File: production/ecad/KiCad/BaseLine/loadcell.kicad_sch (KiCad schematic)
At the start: 10 parts, among them J1 LoadCell Connector, U1 ADS122C04IPW

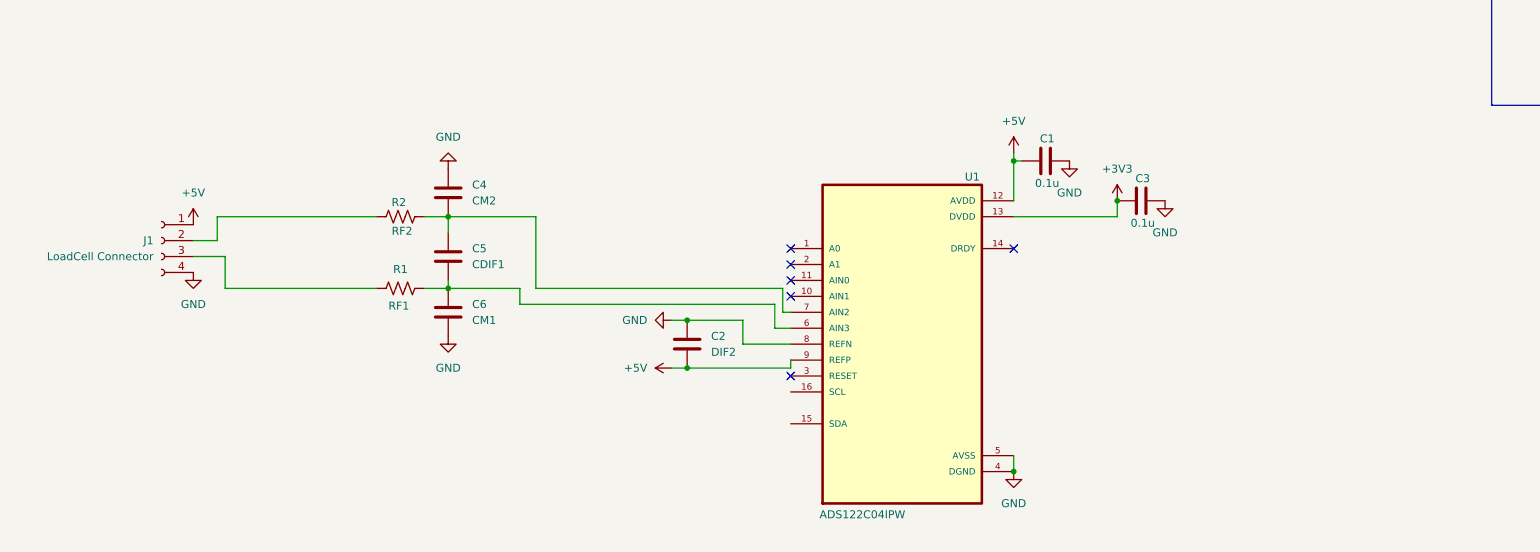
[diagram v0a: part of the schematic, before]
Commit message: Added vibe motor connector and amp I2C
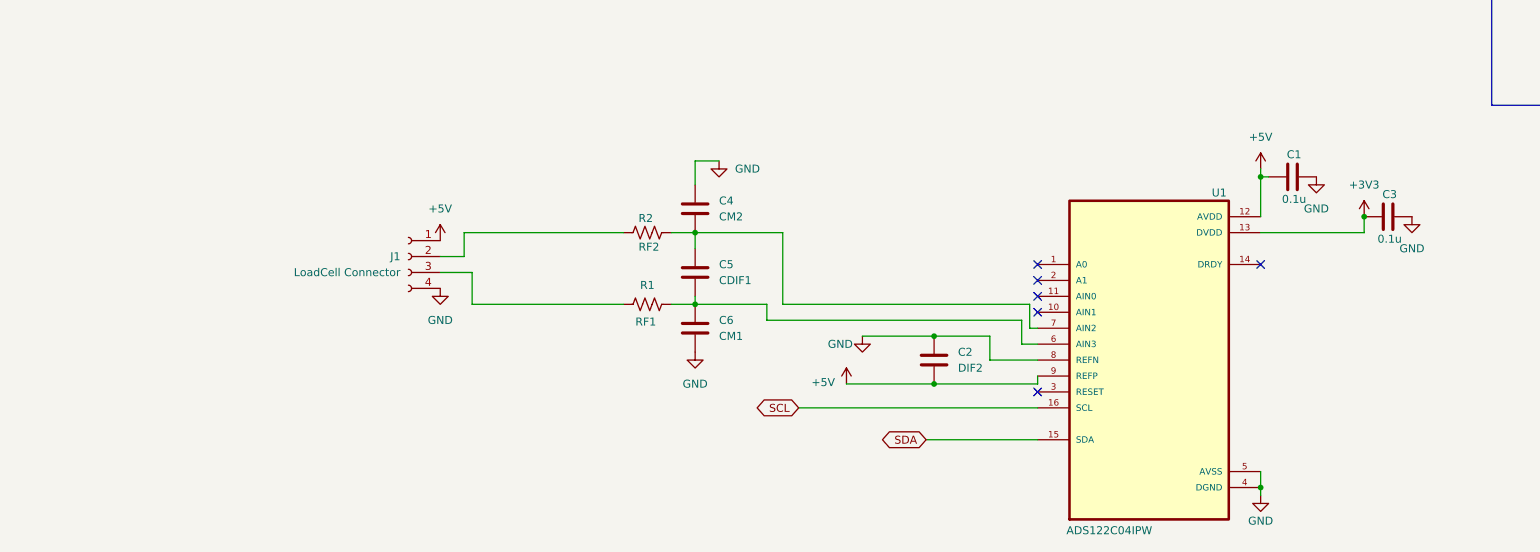
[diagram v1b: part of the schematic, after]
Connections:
- net SDA: now reaches U1.15 (SDA)
- net SCL: now reaches U1.16 (SCL)
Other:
- moved on the sheet: C1, C2, C3, C4, C5, C6, J1, R1, R2, U1

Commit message: Small changes
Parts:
- J1: value LoadCell Connector -> FX1901-0001-0200-L
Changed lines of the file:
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@@
 			)
 		)
-		(property "Value" "LoadCell Connector"
+		(property "Value" "FX1901-0001-0200-L"
 			(at 66.04 88.8999 0)
 			(effects
@@
 			)
 		)
-		(property "Datasheet" "~"
+		(property "Datasheet" "https://www.digikey.com/en/products/detail/te-connectivity-measurement-specialties/FX1901-0001-0200-L/5277314"
 			(at 67.31 86.36 0)
 			(effects

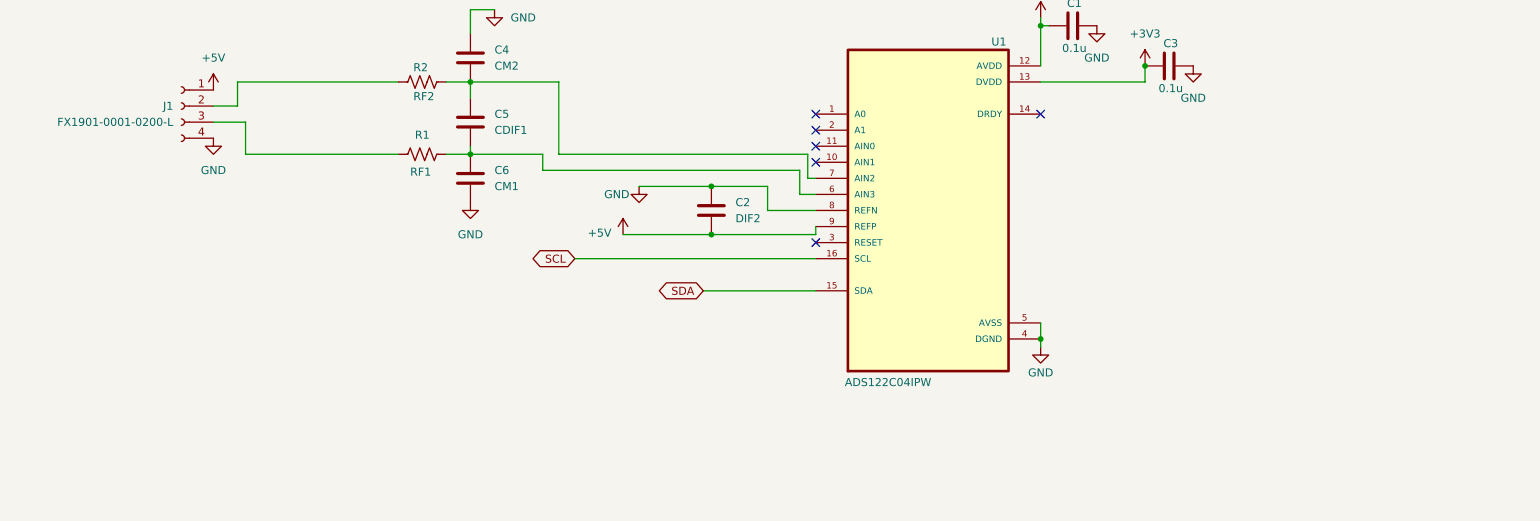
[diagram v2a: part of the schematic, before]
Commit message: Updated with new load cell amp IC
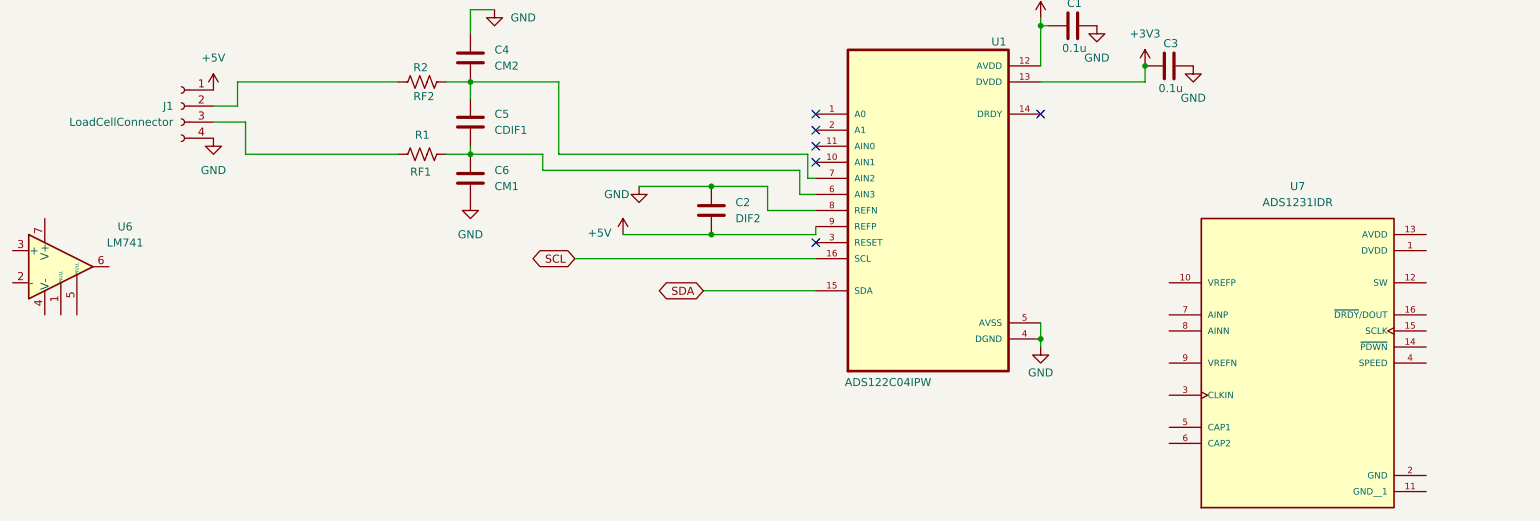
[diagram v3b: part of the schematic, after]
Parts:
- added U6: LM741, symbol Amplifier_Operational:LM741
- added U7: ADS1231IDR, ADS1231IDR:SOIC127P600X175-16N, symbol ADS1231IDR:ADS1231IDR
- J1: value FX1901-0001-0200-L -> LoadCellConnector

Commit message: Load Cell changes
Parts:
- removed C1, C3: 0.1u, symbol Device:C
- removed C2: DIF2, symbol Device:C
- removed C4: CM2, symbol Device:C
- removed C5: CDIF1, symbol Device:C
- removed C6: CM1, symbol Device:C
- removed R1: RF1, symbol Device:R_US
- removed R2: RF2, symbol Device:R_US
- removed U1: ADS122C04IPW, ADS122C04IPW:SOP65P640X120-16N, symbol ADS122C04IPW:ADS122C04IPW
- removed U6: LM741, symbol Amplifier_Operational:LM741
- added C16, C17: C, symbol Device:C
- added R23, R24, R25, R26: R_US, symbol Device:R_US
- added U6, U8: MIC920YC5-TR, SC-70_C5_MCH, symbol 2024-10-08_01-43-59:MIC920YC5-TR
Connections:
- net +5V: now also U6.5 (V+), U8.5 (V+)
- net GND: now also U6.2 (V-), U8.2 (V-)
- net RawLoadCell_-: now reaches J1.3 (Pin_3)
- net RawLoadCell_-: now also R25.2
- net RawLoadCell_+: now reaches J1.2 (Pin_2)
- net RawLoadCell_+: now also R23.2
- net LP_+: now reaches U7.7 (AINP)
- net LP_+: now also C16.2, U8.3 (IN-), U8.4 (OUT)
- net LP_-: now reaches U7.8 (AINN)
- net LP_-: now also C17.2, U6.3 (IN-), U6.4 (OUT)
- new net: R26.1, U6.1 (IN+)
- new net: C17.1, R25.1, R26.2
- new net: C16.1, R23.1, R24.2
- new net: R24.1, U8.1 (IN+)
- no-connect marks 6 -> 0
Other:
- note added: "Load Cell Low Pass Filtering"
- moved on the sheet: J1, U7

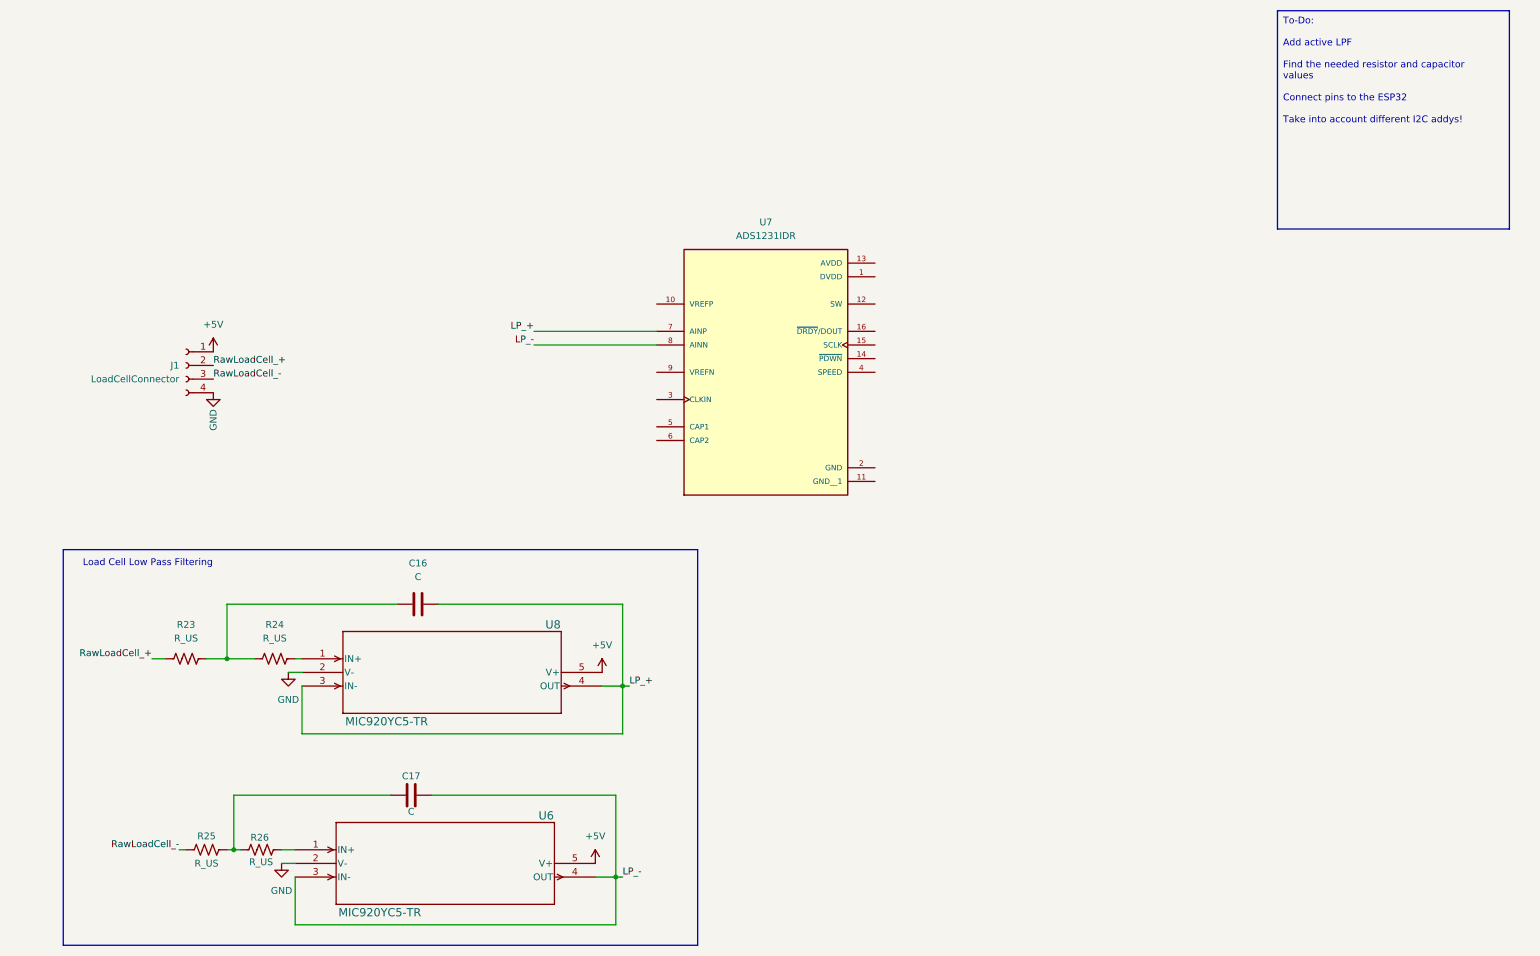
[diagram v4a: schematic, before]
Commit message: Added load cell amp schematic
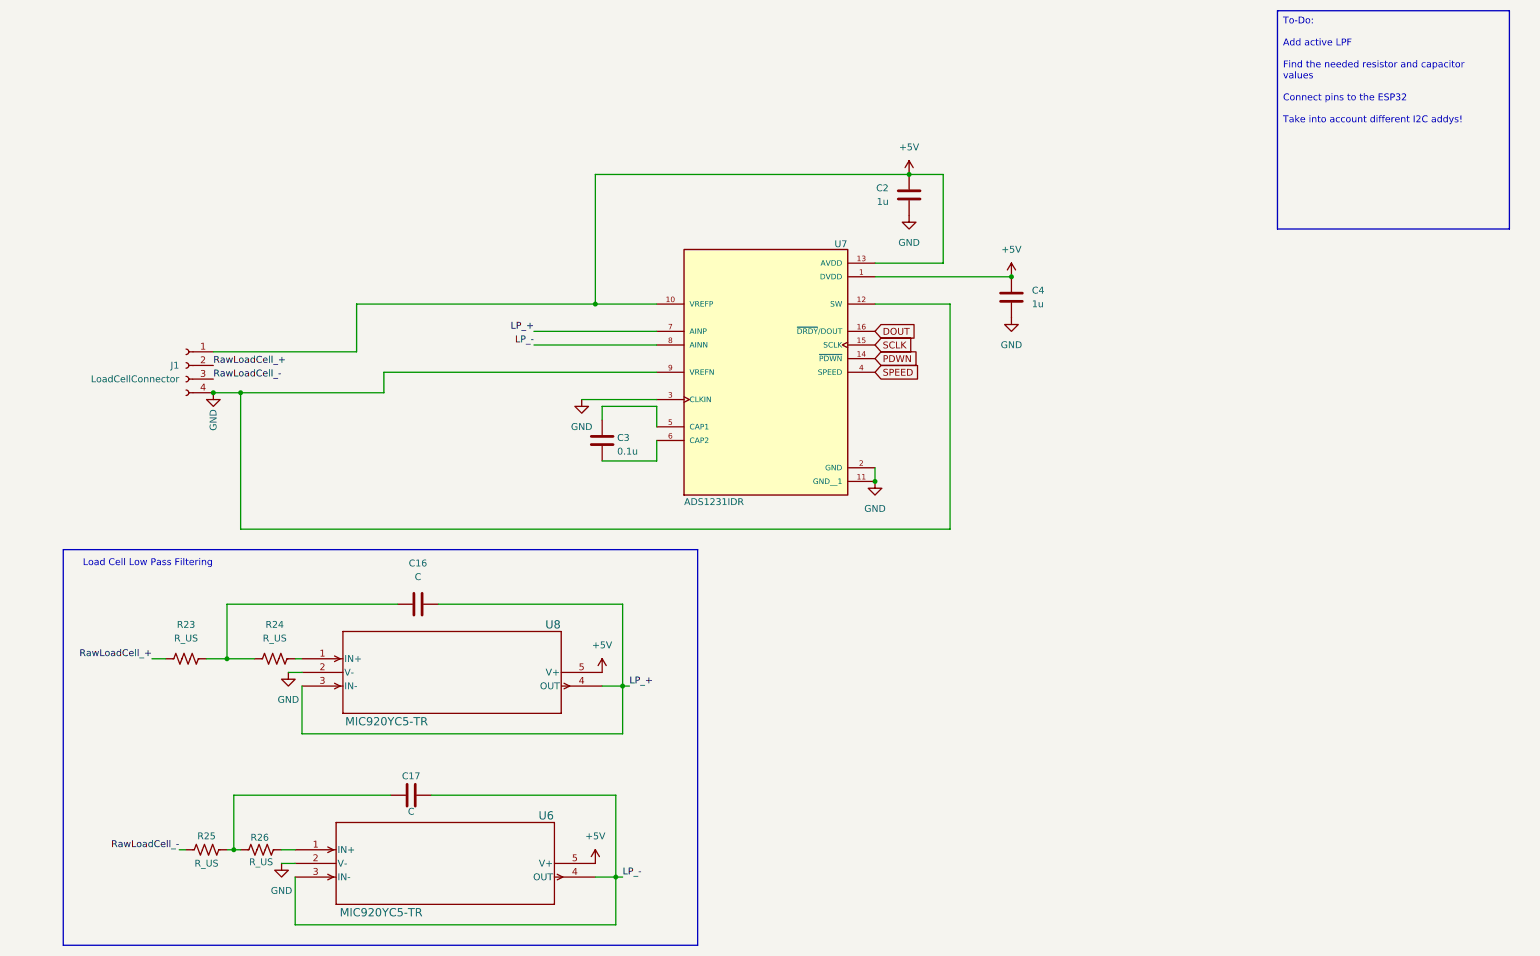
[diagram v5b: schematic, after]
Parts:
- added C2, C4: 1u, symbol Device:C
- added C3: 0.1u, symbol Device:C
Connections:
- net +5V: now also U7.1 (DVDD), U7.10 (VREFP), U7.13 (AVDD), C2.1, C4.1
- net GND: now also U7.11 (GND__1), U7.12 (SW), U7.2 (GND), U7.3 (CLKIN), U7.9 (VREFN), C2.2, C4.2
- net PDWN: now reaches U7.14 (~{PDWN})
- net SCLK: now reaches U7.15 (SCLK)
- net DOUT: now reaches U7.16 (~{DRDY}/DOUT)
- net SPEED: now reaches U7.4 (SPEED)
- net at U7.5 (CAP1): now also C3.1
- net at U7.6 (CAP2): now also C3.2

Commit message: Updates
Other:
- note removed: "Load Cell Low Pass Filtering"
- moved on the sheet: C2
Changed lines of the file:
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@@
 	)
 	(junction
-		(at 45.72 177.8)
+		(at 73.66 92.71)
 		(diameter 0)
 		(color 0 0 0 0)
 	)
 	(junction
-		(at 171.45 52.07)
+		(at 45.72 177.8)
 		(diameter 0)
 		(color 0 0 0 0)
@@
 	)
 	(junction
-		(at 46.99 92.71)
+		(at 177.8 52.07)
+		(diameter 0)
+		(color 0 0 0 0)
+	)
+	(junction
+		(at 185.42 52.07)
 		(diameter 0)
 		(color 0 0 0 0)
@@
 	(wire
 		(pts
+			(xy 185.42 52.07) (xy 177.8 52.07)
+		)
+		(stroke
+			(width 0)
+			(type default)
+		)
+	)
+	(wire
+		(pts
 			(xy 57.15 142.24) (xy 58.42 142.24)
 		)
@@
 	(wire
 		(pts
-			(xy 113.03 52.07) (xy 171.45 52.07)
+			(xy 113.03 52.07) (xy 177.8 52.07)
 		)
 		(stroke
@@
 	(wire
 		(pts
-			(xy 46.99 92.71) (xy 41.91 92.71)
+			(xy 41.91 92.71) (xy 73.66 92.71)
 		)
 		(stroke
@@
 	(wire
 		(pts
-			(xy 73.66 88.9) (xy 73.66 92.71)
+			(xy 73.66 88.9) (xy 124.46 88.9)
 		)
 		(stroke
@@
 	(wire
 		(pts
-			(xy 73.66 92.71) (xy 46.99 92.71)
+			(xy 114.3 97.79) (xy 114.3 95.25)
 		)
 		(stroke
@@
 	(wire
 		(pts
-			(xy 114.3 97.79) (xy 114.3 95.25)
+			(xy 57.15 182.88) (xy 57.15 191.77)
 		)
 		(stroke
@@
 	(wire
 		(pts
-			(xy 57.15 182.88) (xy 57.15 191.77)
+			(xy 30.48 142.24) (xy 33.02 142.24)
 		)
 		(stroke
@@
 	(wire
 		(pts
-			(xy 30.48 142.24) (xy 33.02 142.24)
+			(xy 40.64 142.24) (xy 44.45 142.24)
 		)
 		(stroke
@@
 	(wire
 		(pts
-			(xy 40.64 142.24) (xy 44.45 142.24)
+			(xy 165.1 71.12) (xy 190.5 71.12)
 		)
 		(stroke
@@
 	(wire
 		(pts
-			(xy 165.1 71.12) (xy 190.5 71.12)
+			(xy 116.84 182.88) (xy 116.84 191.77)
 		)
 		(stroke
@@
 	(wire
 		(pts
-			(xy 116.84 182.88) (xy 116.84 191.77)
+			(xy 73.66 92.71) (xy 73.66 88.9)
 		)
 		(stroke
@@
 	(wire
 		(pts
-			(xy 179.07 118.11) (xy 46.99 118.11)
+			(xy 179.07 118.11) (xy 73.66 118.11)
 		)
 		(stroke
@@
 	(wire
 		(pts
-			(xy 124.46 88.9) (xy 73.66 88.9)
-		)
-		(stroke
-			(width 0)
-			(type default)
-		)
-	)
-	(wire
-		(pts
 			(xy 110.49 93.98) (xy 124.46 93.98)
 		)
@@
 	(wire
 		(pts
-			(xy 46.99 118.11) (xy 46.99 92.71)
+			(xy 73.66 92.71) (xy 73.66 118.11)
 		)
 		(stroke
@@
 	(wire
 		(pts
-			(xy 171.45 52.07) (xy 177.8 52.07)
-		)
-		(stroke
-			(width 0)
-			(type default)
-		)
-	)
-	(wire
-		(pts
 			(xy 101.6 83.82) (xy 124.46 83.82)
 		)
@@
 		)
 	)
-	(rectangle
-		(start 13.97 121.92)
-		(end 132.08 195.58)
-		(stroke
-			(width 0)
-			(type default)
-		)
-		(fill
-			(type none)
-		)
-	)
 	(image
 		(at 64.77 43.18)
@@
 		)
 	)
-	(text_box "To-Do: \n\nAdd active LPF\n\nFind the needed resistor and capacitor values\n\nConnect pins to the ESP32\n\nTake into account different I2C addys!"
+	(text_box "Load Cell Low Pass Filtering\n"
 		(exclude_from_sim no)
-		(at 240.03 21.59 0)
-		(size 43.18 40.64)
+		(at 13.97 120.65 0)
+		(size 120.65 74.93)
 		(stroke
 			(width 0)
@@
 		)
 	)
-	(text "Load Cell Low Pass Filtering"
+	(text_box "To-Do: \n\nFind the needed resistor and capacitor values\n\nHow do you connect to ESP32?\n"
 		(exclude_from_sim no)
-		(at 29.718 124.46 0)
+		(at 240.03 21.59 0)
+		(size 43.18 40.64)
+		(stroke
+			(width 0)
+			(type default)
+		)
+		(fill
+			(type none)
+		)
 		(effects
 			(font
 				(size 1.27 1.27)
 			)
+			(justify left top)
 		)
 	)
@@
 		(on_board yes)
 		(dnp no)
-		(fields_autoplaced yes)
 		(property "Reference" "#PWR051"
 			(at 54.61 186.69 0)
@@
 		)
 		(property "Value" "GND"
-			(at 54.61 185.42 0)
+			(at 54.61 184.15 0)
 			(effects
 				(font
@@
 	)
 	(symbol
+		(lib_name "MIC920YC5-TR_1")
 		(lib_id "2024-10-08_01-43-59:MIC920YC5-TR")
 		(at 58.42 142.24 0)
@@
 	(symbol
 		(lib_id "Device:C")
-		(at 171.45 55.88 0)
+		(at 185.42 55.88 0)
 		(mirror y)
 		(unit 1)
@@
 		(dnp no)
 		(property "Reference" "C2"
-			(at 167.64 54.6099 0)
+			(at 181.61 54.6099 0)
 			(effects
 				(font
@@
 		)
 		(property "Value" "1u"
-			(at 167.64 57.1499 0)
+			(at 181.61 57.1499 0)
 			(effects
 				(font
@@
 		)
 		(property "Footprint" ""
-			(at 170.4848 59.69 0)
+			(at 184.4548 59.69 0)
 			(effects
 				(font
@@
 		)
 		(property "Datasheet" "~"
-			(at 171.45 55.88 0)
+			(at 185.42 55.88 0)
 			(effects
 				(font
@@
 		)
 		(property "Description" "Unpolarized capacitor"
-			(at 171.45 55.88 0)
+			(at 185.42 55.88 0)
 			(effects
 				(font
@@
 		(on_board yes)
 		(dnp no)
-		(fields_autoplaced yes)
 		(property "Reference" "#PWR049"
 			(at 55.88 151.13 0)
@@
 		)
 		(property "Value" "GND"
-			(at 55.88 149.86 0)
+			(at 55.88 148.082 0)
 			(effects
 				(font
@@
 	(symbol
 		(lib_id "power:GND")
-		(at 171.45 59.69 0)
+		(at 185.42 59.69 0)
 		(unit 1)
 		(exclude_from_sim no)
@@
 		(on_board yes)
 		(dnp no)
-		(fields_autoplaced yes)
 		(property "Reference" "#PWR04"
-			(at 171.45 66.04 0)
+			(at 185.42 66.04 0)
 			(effects
 				(font
@@
 		)
 		(property "Value" "GND"
-			(at 171.45 64.77 0)
+			(at 185.674 63.754 0)
 			(effects
 				(font
@@
 		)
 		(property "Footprint" ""
-			(at 171.45 59.69 0)
+			(at 185.42 59.69 0)
 			(effects
 				(font
@@
 		)
 		(property "Datasheet" ""
-			(at 171.45 59.69 0)
+			(at 185.42 59.69 0)
 			(effects
 				(font
@@
 		)
 		(property "Description" "Power symbol creates a global label with name \"GND\" , ground"
-			(at 171.45 59.69 0)
+			(at 185.42 59.69 0)
 			(effects
 				(font
@@
 		)
 		(property "Value" "GND"
-			(at 41.91 97.79 90)
+			(at 41.91 96.266 0)
 			(effects
 				(font
@@
 	(symbol
 		(lib_id "power:+5V")
-		(at 171.45 52.07 0)
+		(at 185.42 52.07 0)
 		(unit 1)
 		(exclude_from_sim no)
@@
 		(on_board yes)
 		(dnp no)
-		(fields_autoplaced yes)
 		(property "Reference" "#PWR05"
-			(at 171.45 55.88 0)
+			(at 185.42 55.88 0)
 			(effects
 				(font
@@
 		)
 		(property "Value" "+5V"
-			(at 171.45 46.99 0)
+			(at 185.42 46.99 0)
 			(effects
 				(font
@@
 		)
 		(property "Footprint" ""
-			(at 171.45 52.07 0)
+			(at 185.42 52.07 0)
 			(effects
 				(font
@@
 		)
 		(property "Datasheet" ""
-			(at 171.45 52.07 0)
+			(at 185.42 52.07 0)
 			(effects
 				(font
@@
 		)
 		(property "Description" "Power symbol creates a global label with name \"+5V\""
-			(at 171.45 52.07 0)
+			(at 185.42 52.07 0)
 			(effects
 				(font
@@
 			)
 		)
-		(property "Datasheet" ""
+		(property "Datasheet" "https://www.digikey.com/en/products/detail/texas-instruments/ADS1231IDR/2695867"
 			(at 144.78 86.36 0)
 			(effects
